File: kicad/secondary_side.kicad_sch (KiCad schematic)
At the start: 55 parts, among them U1 B179, U2 B179, U3 LM324

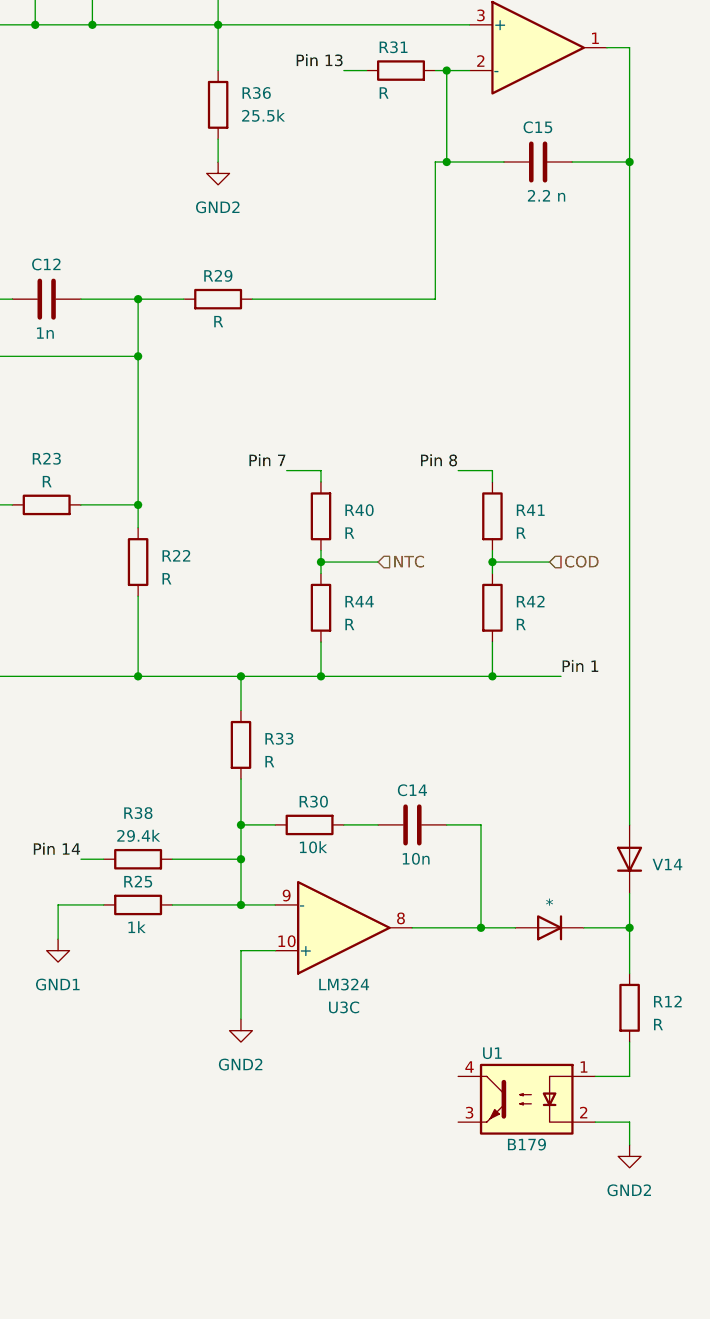
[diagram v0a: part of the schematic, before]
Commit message: Repair resonant circuitry
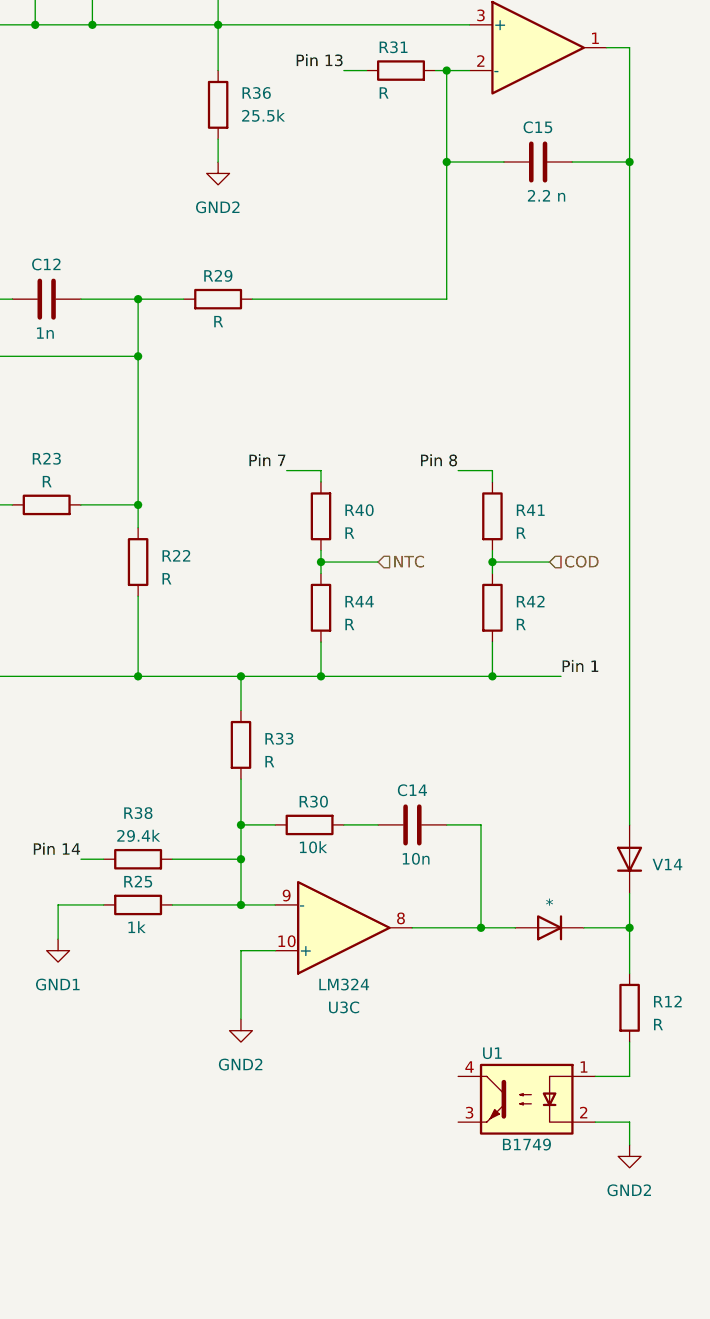
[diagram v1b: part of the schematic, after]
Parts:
- U1: value B179 -> B1749
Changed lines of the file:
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@@
-    (stroke (width 0) (type default))
-  )
-  (wire (pts (xy 246.38 50.8) (xy 247.65 50.8))
     (stroke (width 0) (type default))
   )
@@
     (stroke (width 0) (type default))
   )
-  (wire (pts (xy 246.38 50.8) (xy 246.38 66.04))
-    (stroke (width 0) (type default))
-  )
-  (wire (pts (xy 226.06 66.04) (xy 246.38 66.04))
+  (wire (pts (xy 247.65 50.8) (xy 247.65 66.04))
+    (stroke (width 0) (type default))
+  )
+  (wire (pts (xy 226.06 66.04) (xy 247.65 66.04))
     (stroke (width 0) (type default))
   )
@@
       (effects (font (size 1.27 1.27)))
     )
-    (property "Value" "B179" (at 256.54 160.02 0)
-      (effects (font (size 1.27 1.27)))
-    )
+    (property "Value" "B1749" (at 256.54 160.02 0)
+      (effects (font (size 1.27 1.27)))
+    )

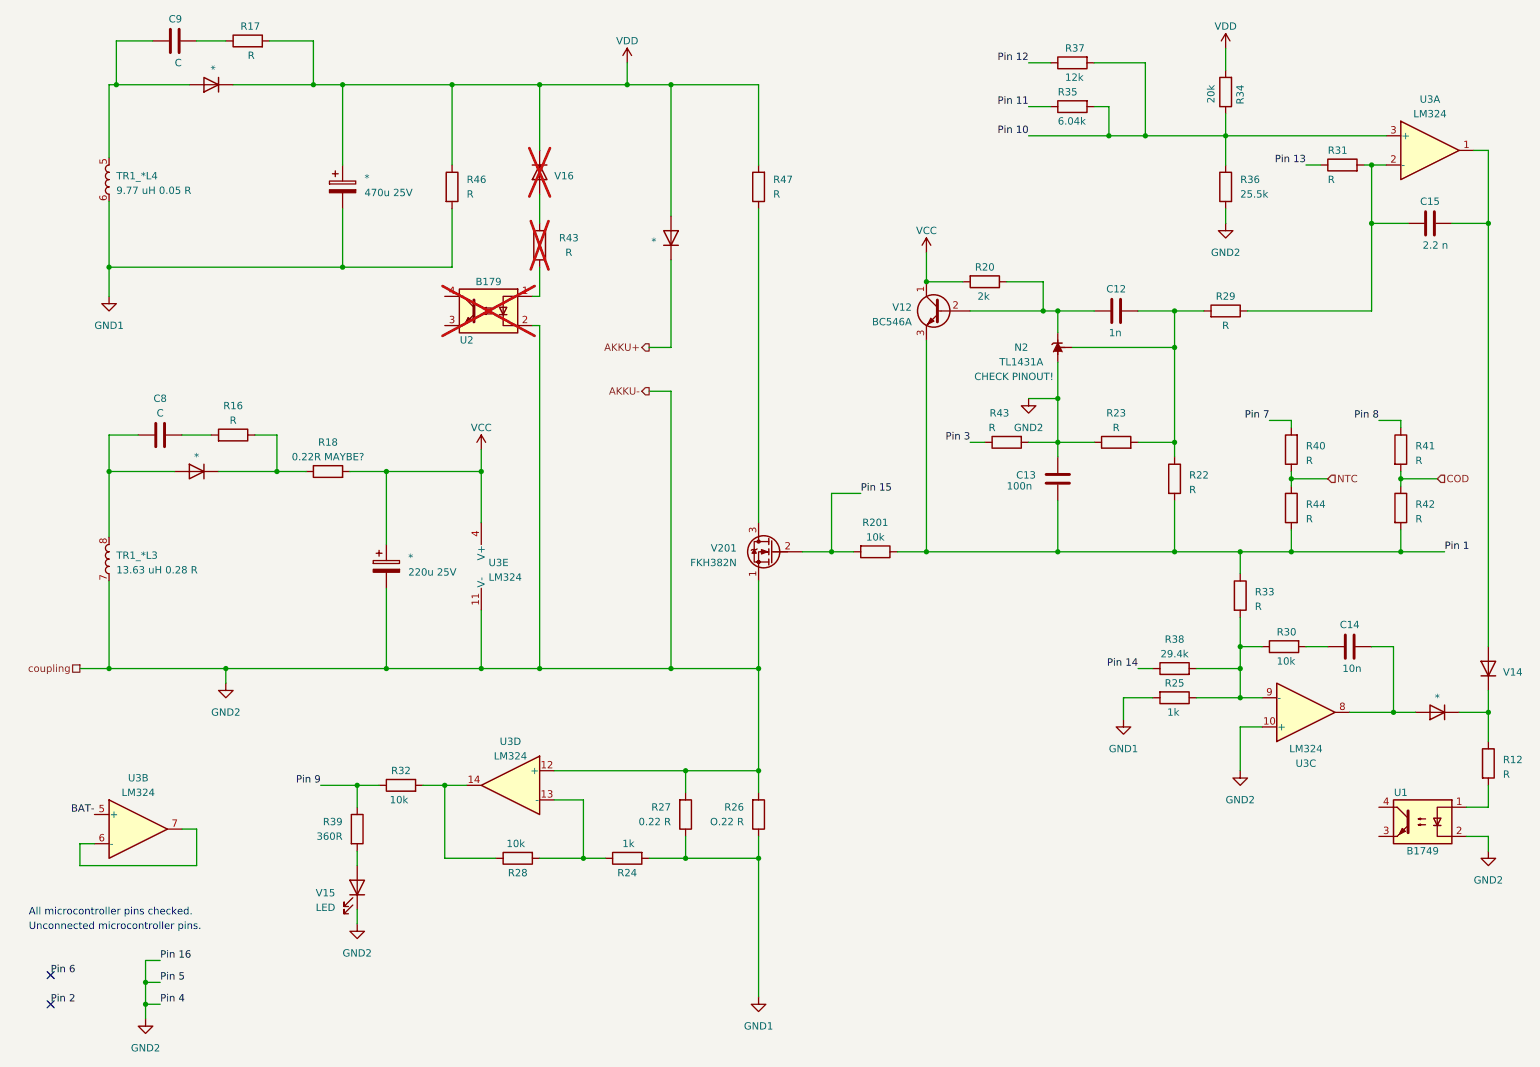
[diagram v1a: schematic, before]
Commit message: Adds dremel battery schematic
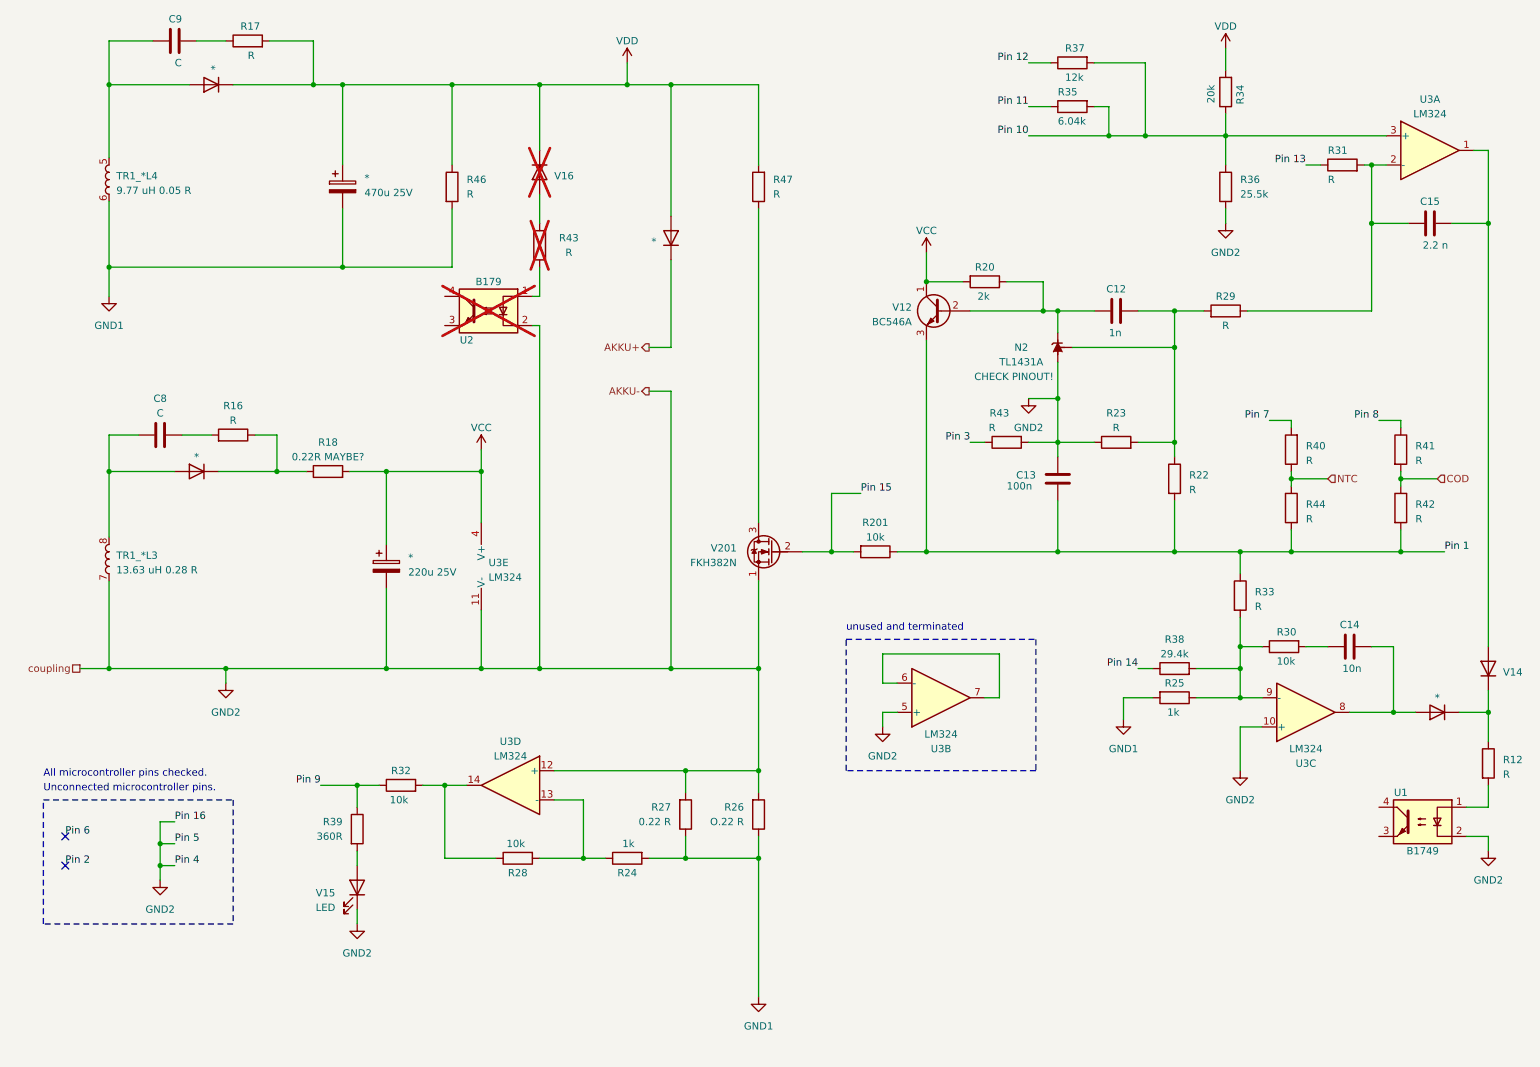
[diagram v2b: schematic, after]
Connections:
- net BAT- is gone; now on net GND2: U3.5 (+)
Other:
- note added: "unused and terminated"
- moved on the sheet: U3B
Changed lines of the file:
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@@
   (junction (at 68.58 58.42) (diameter 0) (color 0 0 0 0)
   )
-  (junction (at 34.29 186.69) (diameter 0) (color 0 0 0 0)
+  (junction (at 36.83 162.56) (diameter 0) (color 0 0 0 0)
   )
   (junction (at 63.5 26.67) (diameter 0) (color 0 0 0 0)
@@
   (junction (at 125.73 128.27) (diameter 0) (color 0 0 0 0)
   )
+  (junction (at 27.94 26.67) (diameter 0) (color 0 0 0 0)
+  )
   (junction (at 140.97 128.27) (diameter 0) (color 0 0 0 0)
   )
@@
   (junction (at 170.18 60.96) (diameter 0) (color 0 0 0 0)
   )
-  (junction (at 34.29 182.88) (diameter 0) (color 0 0 0 0)
+  (junction (at 36.83 158.75) (diameter 0) (color 0 0 0 0)
   )
   (junction (at 213.36 107.95) (diameter 0) (color 0 0 0 0)
@@
   (junction (at 27.94 93.98) (diameter 0) (color 0 0 0 0)
   )
-  (junction (at 29.21 26.67) (diameter 0) (color 0 0 0 0)
-  )
   (junction (at 76.2 128.27) (diameter 0) (color 0 0 0 0)
   )
   (junction (at 224.79 128.27) (diameter 0) (color 0 0 0 0)
   )
-  (no_connect (at 17.78 186.69))
-  (no_connect (at 17.78 181.61))
+  (no_connect (at 20.32 162.56))
+  (no_connect (at 20.32 157.48))
   (wire (pts (xy 102.87 26.67) (xy 102.87 38.1))
     (stroke (width 0) (type default))
@@
     (stroke (width 0) (type default))
   )
-  (wire (pts (xy 43.18 156.21) (xy 40.64 156.21))
+  (wire (pts (xy 182.88 133.35) (xy 180.34 133.35))
     (stroke (width 0) (type default))
   )
@@
     (stroke (width 0) (type default))
   )
-  (wire (pts (xy 29.21 26.67) (xy 41.91 26.67))
-    (stroke (width 0) (type default))
-  )
   (wire (pts (xy 177.8 88.9) (xy 180.34 88.9))
     (stroke (width 0) (type default))
   )
-  (wire (pts (xy 34.29 182.88) (xy 34.29 186.69))
+  (wire (pts (xy 36.83 158.75) (xy 36.83 162.56))
     (stroke (width 0) (type default))
   )
@@
     (stroke (width 0) (type default))
   )
-  (wire (pts (xy 43.18 162.56) (xy 43.18 156.21))
+  (wire (pts (xy 182.88 125.73) (xy 182.88 133.35))
     (stroke (width 0) (type default))
   )
@@
     (stroke (width 0) (type default))
   )
-  (wire (pts (xy 36.83 179.07) (xy 34.29 179.07))
+  (wire (pts (xy 39.37 154.94) (xy 36.83 154.94))
     (stroke (width 0) (type default))
   )
@@
     (stroke (width 0) (type default))
   )
-  (wire (pts (xy 25.4 158.75) (xy 22.86 158.75))
+  (wire (pts (xy 165.1 130.81) (xy 162.56 130.81))
     (stroke (width 0) (type default))
   )
@@
     (stroke (width 0) (type default))
   )
-  (wire (pts (xy 36.83 182.88) (xy 34.29 182.88))
+  (wire (pts (xy 39.37 158.75) (xy 36.83 158.75))
     (stroke (width 0) (type default))
   )
@@
     (stroke (width 0) (type default))
   )
-  (wire (pts (xy 34.29 186.69) (xy 36.83 186.69))
+  (wire (pts (xy 36.83 162.56) (xy 39.37 162.56))
     (stroke (width 0) (type default))
   )
@@
     (stroke (width 0) (type default))
   )
-  (wire (pts (xy 34.29 179.07) (xy 34.29 182.88))
+  (wire (pts (xy 36.83 154.94) (xy 36.83 158.75))
     (stroke (width 0) (type default))
   )
@@
     (stroke (width 0) (type default))
   )
-  (wire (pts (xy 22.86 158.75) (xy 22.86 162.56))
+  (wire (pts (xy 162.56 130.81) (xy 162.56 125.73))
     (stroke (width 0) (type default))
   )
@@
     (stroke (width 0) (type default))
   )
-  (wire (pts (xy 27.94 26.67) (xy 29.21 26.67))
+  (wire (pts (xy 27.94 26.67) (xy 41.91 26.67))
     (stroke (width 0) (type default))
   )
@@
     (stroke (width 0) (type default))
   )
+  (wire (pts (xy 162.56 138.43) (xy 162.56 135.89))
+    (stroke (width 0) (type default))
+  )
   (wire (pts (xy 140.97 146.05) (xy 140.97 149.86))
     (stroke (width 0) (type default))
@@
     (stroke (width 0) (type default))
   )
+  (wire (pts (xy 162.56 135.89) (xy 165.1 135.89))
+    (stroke (width 0) (type default))
+  )
   (wire (pts (xy 193.04 74.93) (xy 193.04 81.28))
     (stroke (width 0) (type default))
   )
-  (wire (pts (xy 29.21 26.67) (xy 29.21 19.05))
+  (wire (pts (xy 27.94 26.67) (xy 27.94 19.05))
     (stroke (width 0) (type default))
   )
@@
     (stroke (width 0) (type default))
   )
-  (wire (pts (xy 22.86 162.56) (xy 43.18 162.56))
+  (wire (pts (xy 162.56 125.73) (xy 182.88 125.73))
     (stroke (width 0) (type default))
   )
@@
     (stroke (width 0) (type default))
   )
-  (wire (pts (xy 35.56 19.05) (xy 29.21 19.05))
+  (wire (pts (xy 35.56 19.05) (xy 27.94 19.05))
     (stroke (width 0) (type default))
   )
@@
     (stroke (width 0) (type default))
   )
-  (wire (pts (xy 34.29 189.23) (xy 34.29 186.69))
+  (wire (pts (xy 36.83 165.1) (xy 36.83 162.56))
     (stroke (width 0) (type default))
   )
@@
     (stroke (width 0) (type default))
   )
-  (text "Unconnected microcontroller pins." (at 13.97 173.99 0)
+  (rectangle (start 16.51 151.13) (end 49.53 172.72)
+    (stroke (width 0) (type dash))
+    (fill (type none))
+  )
+  (rectangle (start 156.21 123.19) (end 189.23 146.05)
+    (stroke (width 0) (type dash))
+    (fill (type none))
+  )
+  (text "Unconnected microcontroller pins." (at 16.51 149.86 0)
     (effects (font (size 1.27 1.27)) (justify left bottom))
   )
-  (text "All microcontroller pins checked." (at 13.97 171.45 0)
+  (text "All microcontroller pins checked." (at 16.51 147.32 0)
     (effects (font (size 1.27 1.27)) (justify left bottom))
   )
-  (label "BAT-" (at 25.4 153.67 180) (fields_autoplaced)
-    (effects (font (size 1.27 1.27)) (justify right bottom))
-  )
-  (label "Pin 6" (at 17.78 181.61 0) (fields_autoplaced)
+  (text "unused and terminated" (at 156.21 121.92 0)
+    (effects (font (size 1.27 1.27)) (justify left bottom))
+  )
+  (label "Pin 6" (at 20.32 157.48 0) (fields_autoplaced)
     (effects (font (size 1.27 1.27)) (justify left bottom))
   )
@@
     (effects (font (size 1.27 1.27)) (justify right bottom))
   )
-  (label "Pin 16" (at 36.83 179.07 0) (fields_autoplaced)
+  (label "Pin 16" (at 39.37 154.94 0) (fields_autoplaced)
     (effects (font (size 1.27 1.27)) (justify left bottom))
   )
@@
     (effects (font (size 1.27 1.27)) (justify right bottom))
   )
-  (label "Pin 5" (at 36.83 182.88 0) (fields_autoplaced)
+  (label "Pin 5" (at 39.37 158.75 0) (fields_autoplaced)
     (effects (font (size 1.27 1.27)) (justify left bottom))
   )
@@
     (effects (font (size 1.27 1.27)) (justify right bottom))
   )
-  (label "Pin 4" (at 36.83 186.69 0) (fields_autoplaced)
+  (label "Pin 4" (at 39.37 162.56 0) (fields_autoplaced)
     (effects (font (size 1.27 1.27)) (justify left bottom))
   )
-  (label "Pin 2" (at 17.78 186.69 0) (fields_autoplaced)
+  (label "Pin 2" (at 20.32 162.56 0) (fields_autoplaced)
     (effects (font (size 1.27 1.27)) (justify left bottom))
   )
@@
     )
   )
-  (symbol (lib_id "power:GND2") (at 34.29 189.23 0) (unit 1)
-    (in_bom yes) (on_board yes) (dnp no) (fields_autoplaced)
-    (property "Reference" "#PWR01" (at 34.29 195.58 0)
-      (effects (font (size 1.27 1.27)) hide)
-    )
-    (property "Value" "GND2" (at 34.29 194.31 0)
-      (effects (font (size 1.27 1.27)))
-    )
-    (property "Footprint" "" (at 34.29 189.23 0)
-      (effects (font (size 1.27 1.27)) hide)
-    )
-    (property "Datasheet" "" (at 34.29 189.23 0)
+  (symbol (lib_id "power:GND2") (at 36.83 165.1 0) (unit 1)
+    (in_bom yes) (on_board yes) (dnp no) (fields_autoplaced)
+    (property "Reference" "#PWR01" (at 36.83 171.45 0)
+      (effects (font (size 1.27 1.27)) hide)
+    )
+    (property "Value" "GND2" (at 36.83 170.18 0)
+      (effects (font (size 1.27 1.27)))
+    )
+    (property "Footprint" "" (at 36.83 165.1 0)
+      (effects (font (size 1.27 1.27)) hide)
+    )
+    (property "Datasheet" "" (at 36.83 165.1 0)
       (effects (font (size 1.27 1.27)) hide)
     )
@@
     )
   )
+  (symbol (lib_id "power:GND2") (at 162.56 138.43 0) (mirror y) (unit 1)
+    (in_bom yes) (on_board yes) (dnp no) (fields_autoplaced)
+    (property "Reference" "#PWR02" (at 162.56 144.78 0)
+      (effects (font (size 1.27 1.27)) hide)
+    )
+    (property "Value" "GND2" (at 162.56 143.51 0)
+      (effects (font (size 1.27 1.27)))
+    )
+    (property "Footprint" "" (at 162.56 138.43 0)
+      (effects (font (size 1.27 1.27)) hide)
+    )
+    (property "Datasheet" "" (at 162.56 138.43 0)
+      (effects (font (size 1.27 1.27)) hide)
+    )
+    (pin "1")
+    (instances
+      (project "Dremel_PCB1857_V1"
+        (path "/ab18b4c8-6f40-44db-bccd-b69c22b3ada9"
+          (reference "#PWR02") (unit 1)
+        )
+        (path "/ab18b4c8-6f40-44db-bccd-b69c22b3ada9/a48cdbeb-6ee2-4275-8de1-cf332eca272a"
+          (reference "#PWR011") (unit 1)
+        )
+      )
+    )
+  )
   (symbol (lib_id "Isolator:EL817") (at 93.98 66.04 0) (mirror y) (unit 1)
     (in_bom yes) (on_board yes) (dnp yes)
@@
     )
   )
-  (symbol (lib_id "Amplifier_Operational:LM324") (at 33.02 156.21 0) (unit 2)
-    (in_bom yes) (on_board yes) (dnp no) (fields_autoplaced)
-    (property "Reference" "U3" (at 33.02 147.32 0)
-      (effects (font (size 1.27 1.27)))
-    )
-    (property "Value" "LM324" (at 33.02 149.86 0)
-      (effects (font (size 1.27 1.27)))
-    )
-    (property "Footprint" "" (at 31.75 153.67 0)
-      (effects (font (size 1.27 1.27)) hide)
-    )
-    (property "Datasheet" "http://www.ti.com/lit/ds/symlink/lm2902-n.pdf" (at 34.29 151.13 0)
-      (effects (font (size 1.27 1.27)) hide)
-    )
+  (symbol (lib_id "Amplifier_Operational:LM324") (at 172.72 133.35 0) (mirror x) (unit 2)
+    (in_bom yes) (on_board yes) (dnp no) (fields_autoplaced)
+    (property "Reference" "U3" (at 172.72 142.24 0)
+      (effects (font (size 1.27 1.27)))
+    )
+    (property "Value" "LM324" (at 172.72 139.7 0)
+      (effects (font (size 1.27 1.27)))
+    )
+    (property "Footprint" "" (at 171.45 135.89 0)
+      (effects (font (size 1.27 1.27)) hide)
+    )
+    (property "Datasheet" "http://www.ti.com/lit/ds/symlink/lm2902-n.pdf" (at 173.99 138.43 0)
+      (effects (font (size 1.27 1.27)) hide)
+    )
